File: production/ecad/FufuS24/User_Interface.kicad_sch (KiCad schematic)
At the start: 12 parts, among them J3 HDMI_A, J4 USB_B_Micro

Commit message: added PIO and removed CEC
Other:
- note added: "PIO"
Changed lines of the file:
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@@
     (stroke (width 0) (type default))
+  )
+  (text "PIO" (at 139.954 63.373 0)
+    (effects (font (size 1.27 1.27) (color 238 64 255 1)) (justify left bottom))
+  )
+  (text "PIO" (at 139.954 76.2 0)
+    (effects (font (size 1.27 1.27) (color 238 64 255 1)) (justify left bottom))
   )
   (text "uC_DVI_D1-" (at 144.145 68.707 0)
@@
     (effects (font (size 1.27 1.27)) (justify left bottom))
   )
-  (text "uC_DVI_D1+" (at 144.018 66.167 0)
+  (text "PIO" (at 139.954 73.787 0)
+    (effects (font (size 1.27 1.27) (color 238 64 255 1)) (justify left bottom))
+  )
+  (text "PIO" (at 139.954 71.374 0)
+    (effects (font (size 1.27 1.27) (color 238 64 255 1)) (justify left bottom))
+  )
+  (text "PIO" (at 139.954 78.994 0)
+    (effects (font (size 1.27 1.27) (color 238 64 255 1)) (justify left bottom))
+  )
+  (text "uC_DVI_D1+" (at 144.018 65.786 0)
     (effects (font (size 1.27 1.27)) (justify left bottom))
   )
   (text "uC_DVI_SCL" (at 139.446 88.519 0)
     (effects (font (size 1.27 1.27)) (justify left bottom))
+  )
+  (text "PIO" (at 139.954 60.96 0)
+    (effects (font (size 1.27 1.27) (color 238 64 255 1)) (justify left bottom))
+  )
+  (text "PIO" (at 139.954 65.786 0)
+    (effects (font (size 1.27 1.27) (color 238 64 255 1)) (justify left bottom))
   )
   (text "uC_DVI_D0-" (at 144.145 73.787 0)
@@
     (effects (font (size 1.27 1.27)) (justify left bottom))
   )
-  (text "uC_DVI_D2-" (at 143.891 63.627 0)
+  (text "uC_DVI_D2-" (at 144.145 63.246 0)
     (effects (font (size 1.27 1.27)) (justify left bottom))
   )
+  (text "PIO" (at 139.954 68.707 0)
+    (effects (font (size 1.27 1.27) (color 238 64 255 1)) (justify left bottom))
+  )
   (text "uC_DVI_D2+" (at 144.018 60.96 0)

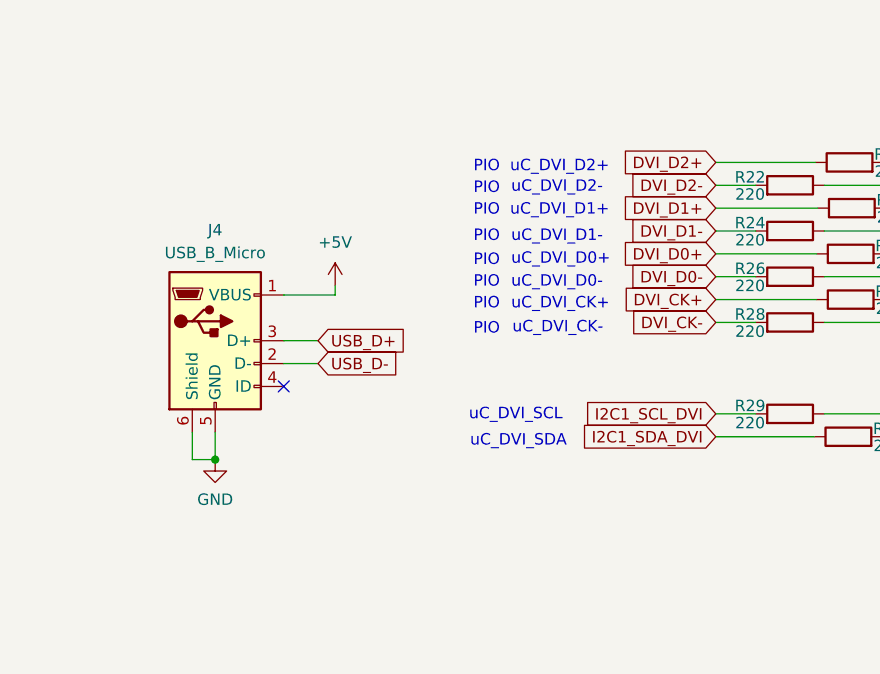
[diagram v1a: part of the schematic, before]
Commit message: Added labels for diff pairs
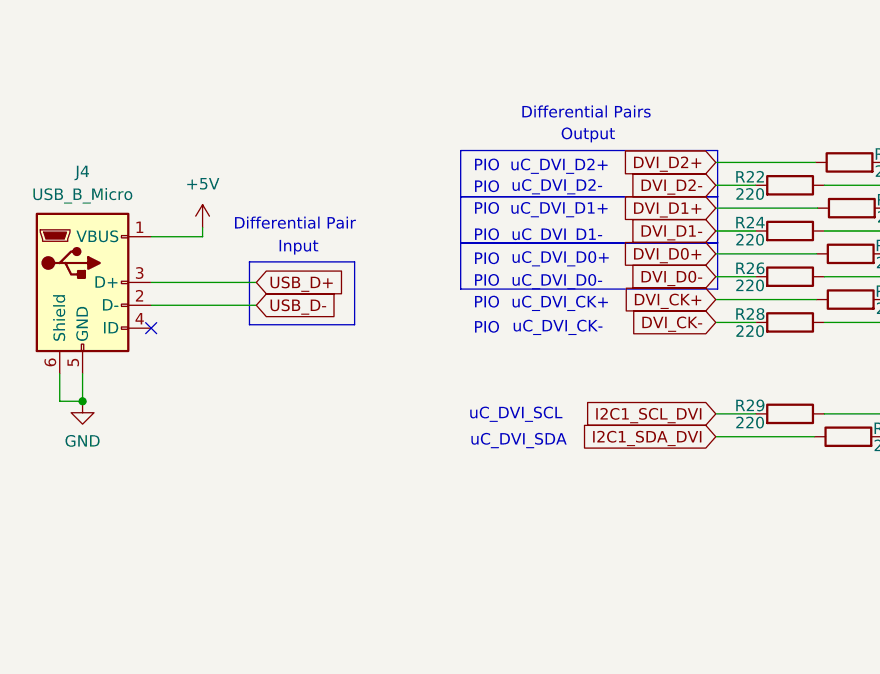
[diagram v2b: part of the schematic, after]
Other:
- note added: "Differential Pair"
- note added: "Differential Pairs"
- note added: "Input"
- note added: "Output"
- moved on the sheet: J4
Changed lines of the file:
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@@
   (junction (at 201.168 110.998) (diameter 0) (color 0 0 0 0)
   )
-  (junction (at 111.252 92.71) (diameter 0) (color 0 0 0 0)
+  (junction (at 96.52 86.233) (diameter 0) (color 0 0 0 0)
   )
   (junction (at 198.628 110.998) (diameter 0) (color 0 0 0 0)
@@
   )
   (no_connect (at 188.468 95.25))
-  (no_connect (at 118.872 84.582))
+  (no_connect (at 104.14 78.105))
   (no_connect (at 188.468 97.79))
   (no_connect (at 188.468 82.55))
@@
     (stroke (width 0) (type default))
   )
-  (wire (pts (xy 118.872 82.042) (xy 122.682 82.042))
-    (stroke (width 0) (type default))
-  )
   (wire (pts (xy 166.878 59.69) (xy 177.927 59.69))
     (stroke (width 0) (type default))
@@
     (stroke (width 0) (type default))
   )
-  (wire (pts (xy 111.252 89.662) (xy 111.252 92.71))
+  (wire (pts (xy 96.52 83.185) (xy 96.52 86.233))
     (stroke (width 0) (type default))
   )
@@
     (stroke (width 0) (type default))
   )
-  (wire (pts (xy 108.712 92.71) (xy 111.252 92.71))
+  (wire (pts (xy 93.98 86.233) (xy 96.52 86.233))
     (stroke (width 0) (type default))
   )
@@
     (stroke (width 0) (type default))
   )
-  (wire (pts (xy 108.712 89.662) (xy 108.712 92.71))
-    (stroke (width 0) (type default))
-  )
-  (wire (pts (xy 118.872 79.502) (xy 122.682 79.502))
-    (stroke (width 0) (type default))
-  )
-  (wire (pts (xy 124.587 74.422) (xy 118.872 74.422))
+  (wire (pts (xy 93.98 83.185) (xy 93.98 86.233))
+    (stroke (width 0) (type default))
+  )
+  (wire (pts (xy 104.14 73.025) (xy 115.824 73.025))
+    (stroke (width 0) (type default))
+  )
+  (wire (pts (xy 109.855 67.945) (xy 104.14 67.945))
+    (stroke (width 0) (type default))
+  )
+  (wire (pts (xy 115.824 75.565) (xy 104.14 75.565))
     (stroke (width 0) (type default))
   )
@@
     (stroke (width 0) (type default))
   )
-  (wire (pts (xy 124.587 73.406) (xy 124.587 74.422))
+  (wire (pts (xy 109.855 66.929) (xy 109.855 67.945))
     (stroke (width 0) (type default))
   )
@@
     (stroke (width 0) (type default))
   )
+  (rectangle (start 115.062 70.739) (end 126.746 77.724)
+    (stroke (width 0) (type default) (color 191 39 255 1))
+    (fill (type none))
+  )
+  (rectangle (start 138.5316 63.5) (end 167.0812 68.6308)
+    (stroke (width 0) (type default) (color 191 39 255 1))
+    (fill (type none))
+  )
+  (rectangle (start 138.5316 68.6308) (end 167.0812 73.7616)
+    (stroke (width 0) (type default) (color 191 39 255 1))
+    (fill (type none))
+  )
+  (rectangle (start 138.5316 58.3692) (end 167.0812 63.5)
+    (stroke (width 0) (type default) (color 191 39 255 1))
+    (fill (type none))
+  )
   (text "PIO" (at 139.954 63.373 0)
     (effects (font (size 1.27 1.27) (color 238 64 255 1)) (justify left bottom))
@@
     (effects (font (size 1.27 1.27) (color 238 64 255 1)) (justify left bottom))
   )
+  (text "Differential Pair\n" (at 113.284 67.437 0)
+    (effects (font (size 1.27 1.27)) (justify left bottom))
+  )
+  (text "Differential Pairs" (at 145.2118 55.0926 0)
+    (effects (font (size 1.27 1.27)) (justify left bottom))
+  )
   (text "PIO" (at 139.954 78.994 0)
     (effects (font (size 1.27 1.27) (color 238 64 255 1)) (justify left bottom))
   )
+  (text "Input\n" (at 118.237 69.977 0)
+    (effects (font (size 1.27 1.27) (color 0 169 62 1)) (justify left bottom))
+  )
   (text "uC_DVI_D1+" (at 144.018 65.786 0)
     (effects (font (size 1.27 1.27)) (justify left bottom))
@@
     (effects (font (size 1.27 1.27)) (justify left bottom))
   )
+  (text "Output\n" (at 149.6568 57.5056 0)
+    (effects (font (size 1.27 1.27) (color 0 169 62 1)) (justify left bottom))
+  )
   (text "PIO" (at 139.954 60.96 0)
     (effects (font (size 1.27 1.27) (color 238 64 255 1)) (justify left bottom))
@@
     )
   )
-  (global_label "USB_D-" (shape input) (at 122.682 82.042 0) (fields_autoplaced)
+  (global_label "USB_D-" (shape input) (at 115.824 75.565 0) (fields_autoplaced)
     (effects (font (size 1.27 1.27)) (justify left))
-    (property "Intersheetrefs" "${INTERSHEET_REFS}" (at 133.2872 82.042 0)
+    (property "Intersheetrefs" "${INTERSHEET_REFS}" (at 126.4292 75.565 0)
       (effects (font (size 1.27 1.27)) (justify left) hide)
     )
@@
     )
   )
-  (global_label "USB_D+" (shape input) (at 122.682 79.502 0) (fields_autoplaced)
+  (global_label "USB_D+" (shape input) (at 115.824 73.025 0) (fields_autoplaced)
     (effects (font (size 1.27 1.27)) (justify left))
-    (property "Intersheetrefs" "${INTERSHEET_REFS}" (at 133.2872 79.502 0)
+    (property "Intersheetrefs" "${INTERSHEET_REFS}" (at 126.4292 73.025 0)
       (effects (font (size 1.27 1.27)) (justify left) hide)
     )
@@
     )
   )
-  (symbol (lib_id "Connector:USB_B_Micro") (at 111.252 79.502 0) (unit 1)
+  (symbol (lib_id "Connector:USB_B_Micro") (at 96.52 73.025 0) (unit 1)
     (in_bom yes) (on_board yes) (dnp no) (fields_autoplaced)
-    (property "Reference" "J4" (at 111.252 67.2084 0)
-      (effects (font (size 1.27 1.27)))
-    )
-    (property "Value" "USB_B_Micro" (at 111.252 69.7484 0)
-      (effects (font (size 1.27 1.27)))
-    )
-    (property "Footprint" "" (at 115.062 80.772 0)
-      (effects (font (size 1.27 1.27)) hide)
-    )
-    (property "Datasheet" "~" (at 115.062 80.772 0)
+    (property "Reference" "J4" (at 96.52 60.7314 0)
+      (effects (font (size 1.27 1.27)))
+    )
+    (property "Value" "USB_B_Micro" (at 96.52 63.2714 0)
+      (effects (font (size 1.27 1.27)))
+    )
+    (property "Footprint" "" (at 100.33 74.295 0)
+      (effects (font (size 1.27 1.27)) hide)
+    )
+    (property "Datasheet" "~" (at 100.33 74.295 0)
       (effects (font (size 1.27 1.27)) hide)
     )
@@
     )
   )
-  (symbol (lib_id "power:+5V") (at 124.587 73.406 0) (unit 1)
+  (symbol (lib_id "power:+5V") (at 109.855 66.929 0) (unit 1)
     (in_bom yes) (on_board yes) (dnp no) (fields_autoplaced)
-    (property "Reference" "#PWR063" (at 124.587 77.216 0)
-      (effects (font (size 1.27 1.27)) hide)
-    )
-    (property "Value" "+5V" (at 124.587 68.58 0)
-      (effects (font (size 1.27 1.27)))
-    )
-    (property "Footprint" "" (at 124.587 73.406 0)
-      (effects (font (size 1.27 1.27)) hide)
-    )
-    (property "Datasheet" "" (at 124.587 73.406 0)
+    (property "Reference" "#PWR063" (at 109.855 70.739 0)
+      (effects (font (size 1.27 1.27)) hide)
+    )
+    (property "Value" "+5V" (at 109.855 62.103 0)
+      (effects (font (size 1.27 1.27)))
+    )
+    (property "Footprint" "" (at 109.855 66.929 0)
+      (effects (font (size 1.27 1.27)) hide)
+    )
+    (property "Datasheet" "" (at 109.855 66.929 0)
       (effects (font (size 1.27 1.27)) hide)
     )
@@
     )
   )
-  (symbol (lib_id "power:GND") (at 111.252 92.71 0) (unit 1)
+  (symbol (lib_id "power:GND") (at 96.52 86.233 0) (unit 1)
     (in_bom yes) (on_board yes) (dnp no) (fields_autoplaced)
-    (property "Reference" "#PWR064" (at 111.252 99.06 0)
-      (effects (font (size 1.27 1.27)) hide)
-    )
-    (property "Value" "GND" (at 111.252 97.155 0)
-      (effects (font (size 1.27 1.27)))
-    )
-    (property "Footprint" "" (at 111.252 92.71 0)
-      (effects (font (size 1.27 1.27)) hide)
-    )
-    (property "Datasheet" "" (at 111.252 92.71 0)
-      (effects (font (size 1.27 1.27)) hide)
-    )
+    (property "Reference" "#PWR064" (at 96.52 92.583 0)
+      (effects (font (size 1.27 1.27)) hide)
+    )
+    (property "Value" "GND" (at 96.52 90.678 0)
+      (effects (font (size 1.27 1.27)))
+    )
+    (property "Footprint" "" (at 96.52 86.233 0)
+      (effects (font (size 1.27 1.27)) hide)
+    )
+    (property "Datasheet" "" (at 96.52 86.233 0)
+      (effects (font (size 1.27 1.27)) hide)
+    )

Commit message: Added feedback notes
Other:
- note added: "add decoupling caps and ESD protections between hdmi power and flag"
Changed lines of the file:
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@@
     (stroke (width 0) (type default))
+  )
+  (rectangle (start 138.5316 73.7108) (end 167.0812 78.8416)
+    (stroke (width 0) (type default) (color 191 39 255 1))
+    (fill (type none))
   )
   (rectangle (start 115.062 70.739) (end 126.746 77.724)
@@
   (rectangle (start 138.5316 63.5) (end 167.0812 68.6308)
     (stroke (width 0) (type default) (color 191 39 255 1))
+    (fill (type none))
+  )
+  (rectangle (start 89.408 105.8164) (end 179.324 123.0884)
+    (stroke (width 0) (type default))
     (fill (type none))
   )
@@
     (effects (font (size 1.27 1.27) (color 238 64 255 1)) (justify left bottom))
   )
+  (text "add decoupling caps and ESD protections between hdmi power and flag"
+    (at 98.3996 112.1664 0)
+    (effects (font (size 1.27 1.27) (color 0 0 0 1)) (justify left bottom))
+  )
   (text "Input\n" (at 118.237 69.977 0)

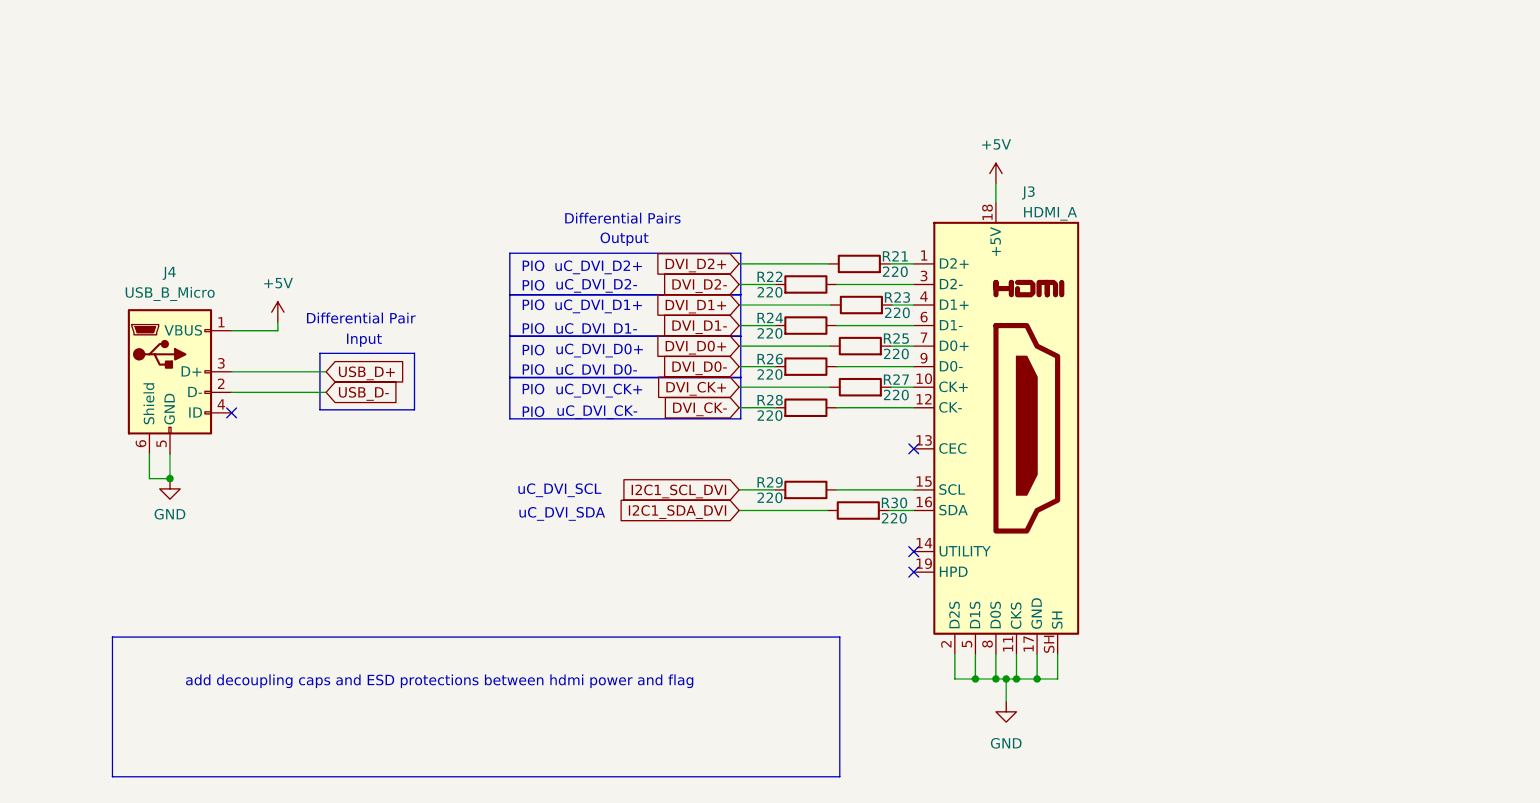
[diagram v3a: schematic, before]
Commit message: Added coupling caps to HDMI
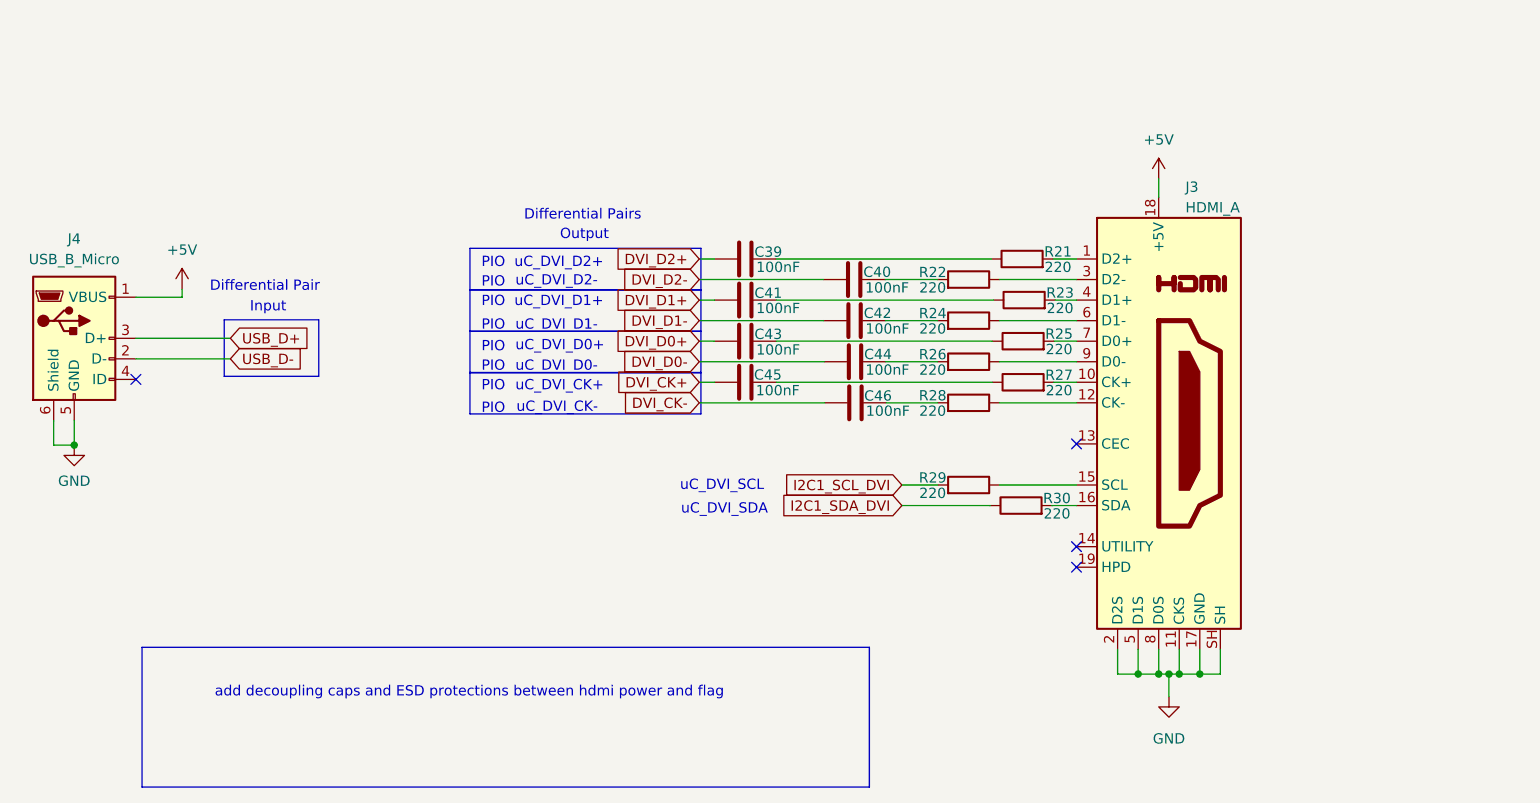
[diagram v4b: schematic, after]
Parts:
- added C39, C40, C41, C42, C43, C44, C45, C46: 100nF, symbol Device:C
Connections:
- net DVI_CK+: now also C45.1; no longer R27.1
- net DVI_CK-: now also C46.1; no longer R28.2
- net DVI_D0+: now also C43.1; no longer R25.1
- net DVI_D0-: now also C44.1; no longer R26.2
- net DVI_D1+: now also C41.1; no longer R23.1
- net DVI_D1-: now also C42.1; no longer R24.2
- net DVI_D2+: now also C39.1; no longer R21.1
- net DVI_D2-: now also C40.1; no longer R22.2
- new net: C45.2, R27.1
- new net: C40.2, R22.2
- new net: C42.2, R24.2
- new net: C39.2, R21.1
- new net: C44.2, R26.2
- new net: C41.2, R23.1
- new net: C46.2, R28.2
- new net: C43.2, R25.1
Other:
- moved on the sheet: J3, J4, R21, R22, R23, R24, R25, R26, R27, R28, R29, R30
